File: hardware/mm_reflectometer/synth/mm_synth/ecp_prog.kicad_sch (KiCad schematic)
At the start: 77 parts, among them J1601 USB_C_Receptacle_USB2.0, J1603 JTAG, J1604 Flash, SW1601 SW_Push, SW1602 SW_Push, U1601 ECP5U_25_CABGA256, U1602 93LC56C, U1603 TPD3S014, U1604 FT2232HQ, U1605 W25Q32JVSS, Y1601 7M-12.000MAAJ

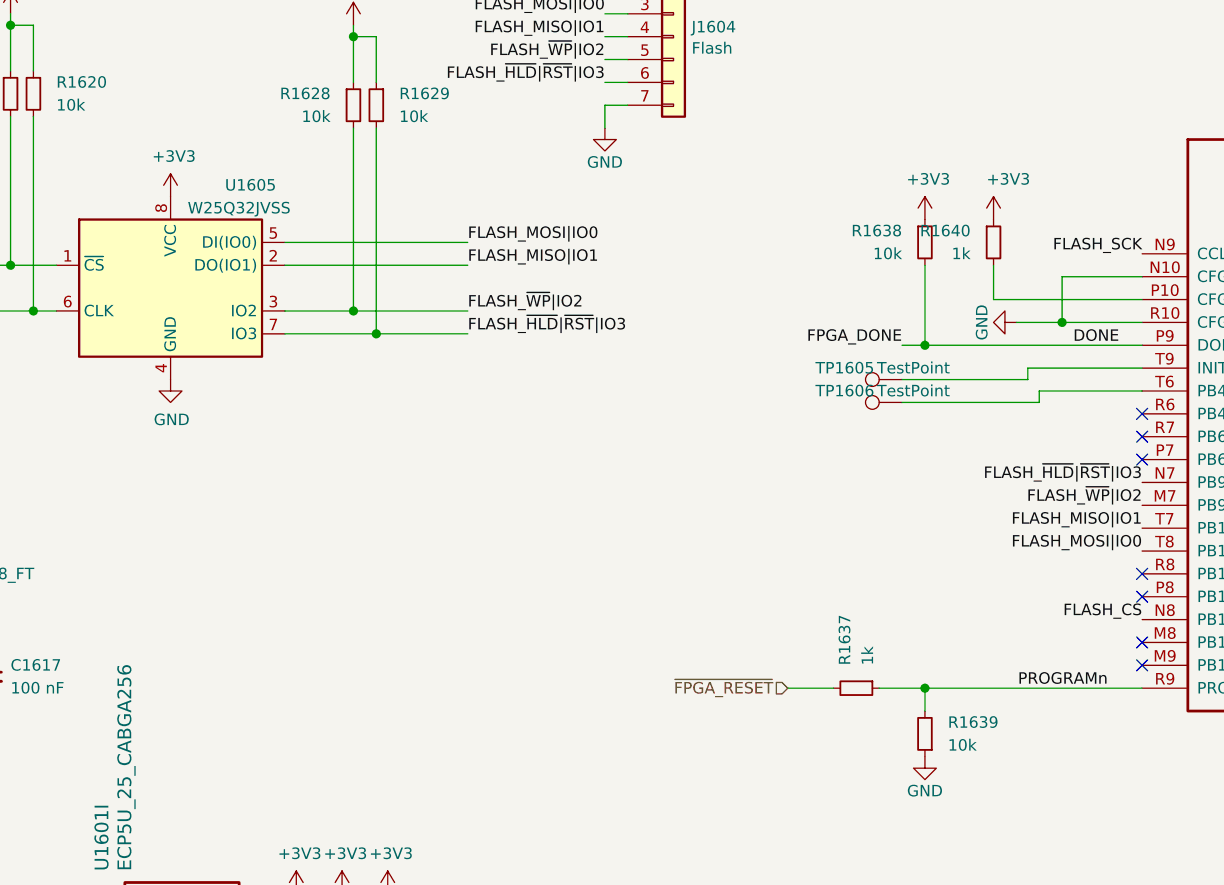
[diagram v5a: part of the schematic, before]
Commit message: created HUSB238 eval board, added clock splitter to mm synth
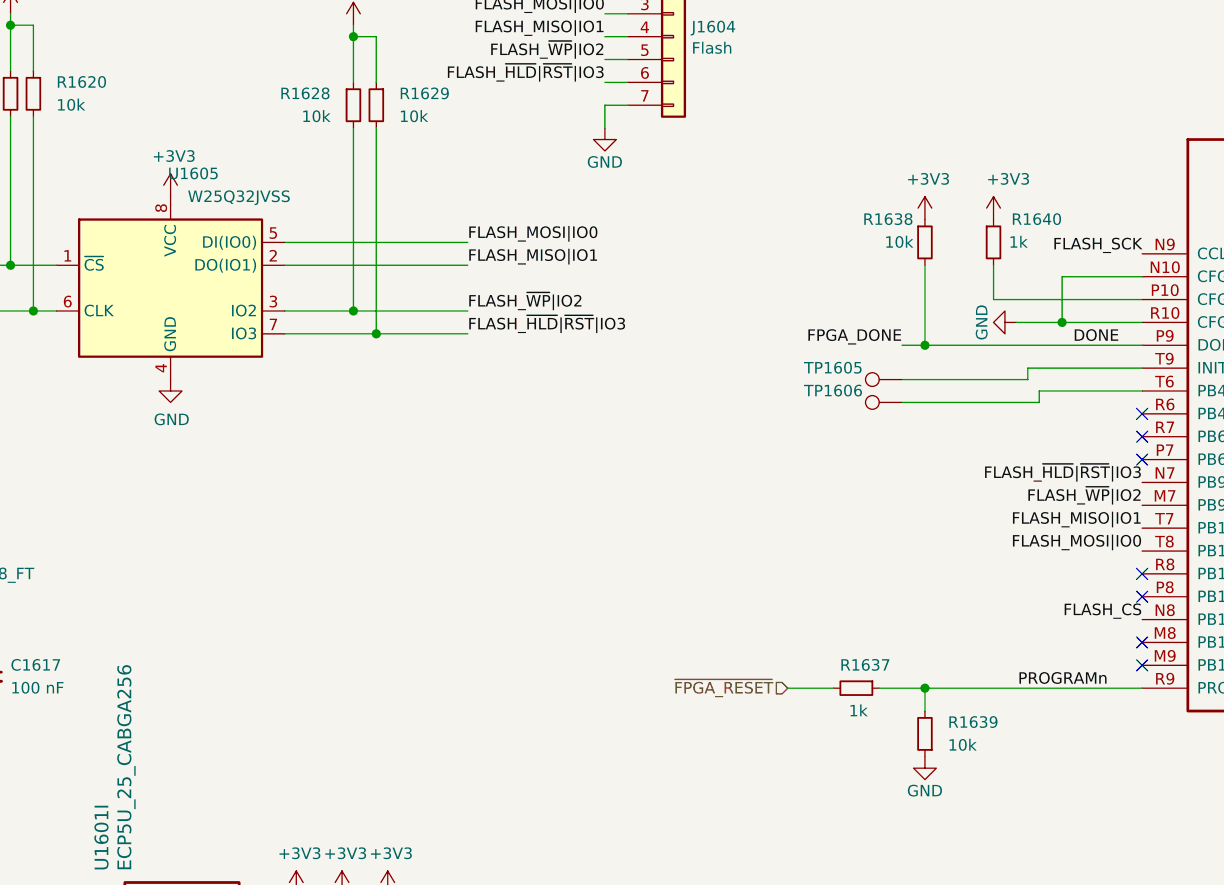
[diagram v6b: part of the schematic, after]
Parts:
- TP1605, TP1606: now left out of the parts list
- U1605: footprint Package_SON:WSON-8-1EP_6x5mm_P1.27mm_EP3.4x4mm -> Package_SO:SOIC-8_5.23x5.23mm_P1.27mm; Notes Flash schematic and symbol adapted from Greg Davill's ECPBr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 -> (none)
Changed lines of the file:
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@@
   )
   (symbol (lib_id "Connector:TestPoint") (at 280.67 67.31 90) (unit 1)
-    (in_bom yes) (on_board yes)
-    (property "Reference" "TP1605" (id 0) (at 274.32 66.04 90))
-    (property "Value" "TestPoint" (id 1) (at 281.94 66.04 90))
+    (in_bom no) (on_board yes)
+    (property "Reference" "TP1605" (id 0) (at 273.05 66.04 90))
+    (property "Value" "TestPoint" (id 1) (at 283.21 66.04 90)
+      (effects (font (size 1.27 1.27)) hide)
+    )
     (property "Footprint" "TestPoint:TestPoint_Pad_D1.5mm" (id 2) (at 280.67 62.23 0)
       (effects (font (size 1.27 1.27)) hide)
@@
   )
   (symbol (lib_id "Connector:TestPoint") (at 280.67 69.85 90) (unit 1)
-    (in_bom yes) (on_board yes)
-    (property "Reference" "TP1606" (id 0) (at 274.32 68.58 90))
-    (property "Value" "TestPoint" (id 1) (at 281.94 68.58 90))
+    (in_bom no) (on_board yes)
+    (property "Reference" "TP1606" (id 0) (at 273.05 68.58 90))
+    (property "Value" "TestPoint" (id 1) (at 281.94 68.58 90)
+      (effects (font (size 1.27 1.27)) hide)
+    )
     (property "Footprint" "TestPoint:TestPoint_Pad_D1.5mm" (id 2) (at 280.67 64.77 0)
       (effects (font (size 1.27 1.27)) hide)
@@
   (symbol (lib_id "Device:R_Small") (at 275.59 101.6 270) (unit 1)
     (in_bom yes) (on_board yes)
-    (property "Reference" "R1637" (id 0) (at 274.32 99.06 0)
-      (effects (font (size 1.27 1.27)) (justify right))
-    )
-    (property "Value" "1k" (id 1) (at 276.86 99.06 0)
+    (property "Reference" "R1637" (id 0) (at 279.4 99.06 90)
+      (effects (font (size 1.27 1.27)) (justify right))
+    )
+    (property "Value" "1k" (id 1) (at 276.86 104.14 90)
       (effects (font (size 1.27 1.27)) (justify right))
     )
@@
   (symbol (lib_id "Device:R_Small") (at 283.21 52.07 0) (unit 1)
     (in_bom yes) (on_board yes)
-    (property "Reference" "R1638" (id 0) (at 280.67 50.8 0)
-      (effects (font (size 1.27 1.27)) (justify right))
-    )
-    (property "Value" "10k" (id 1) (at 280.67 53.34 0)
+    (property "Reference" "R1638" (id 0) (at 281.94 49.53 0)
+      (effects (font (size 1.27 1.27)) (justify right))
+    )
+    (property "Value" "10k" (id 1) (at 281.94 52.07 0)
       (effects (font (size 1.27 1.27)) (justify right))
     )
@@
   (symbol (lib_id "Device:R_Small") (at 290.83 52.07 0) (unit 1)
     (in_bom yes) (on_board yes)
-    (property "Reference" "R1640" (id 0) (at 288.29 50.8 0)
-      (effects (font (size 1.27 1.27)) (justify right))
-    )
-    (property "Value" "1k" (id 1) (at 288.29 53.34 0)
+    (property "Reference" "R1640" (id 0) (at 298.45 49.53 0)
+      (effects (font (size 1.27 1.27)) (justify right))
+    )
+    (property "Value" "1k" (id 1) (at 294.64 52.07 0)
       (effects (font (size 1.27 1.27)) (justify right))
     )
@@
   (symbol (lib_id "Memory_Flash:W25Q32JVSS") (at 199.39 57.15 0) (unit 1)
     (in_bom yes) (on_board yes)
-    (property "Reference" "U1605" (id 0) (at 208.28 45.72 0))
-    (property "Value" "W25Q32JVSS" (id 1) (at 207.01 48.26 0))
-    (property "Footprint" "Package_SON:WSON-8-1EP_6x5mm_P1.27mm_EP3.4x4mm" (id 2) (at 199.39 57.15 0)
+    (property "Reference" "U1605" (id 0) (at 201.93 44.45 0))
+    (property "Value" "W25Q32JVSS" (id 1) (at 207.01 46.99 0))
+    (property "Footprint" "Package_SO:SOIC-8_5.23x5.23mm_P1.27mm" (id 2) (at 199.39 57.15 0)
       (effects (font (size 1.27 1.27)) hide)
     )
@@
       (effects (font (size 1.27 1.27)) hide)
     )
-    (property "Notes" "Flash schematic and symbol adapted from Greg Davill's ECPBreaker, CC-BY-SA V4.0" (id 4) (at 199.39 57.15 0)
-      (effects (font (size 1.27 1.27)) hide)
-    )

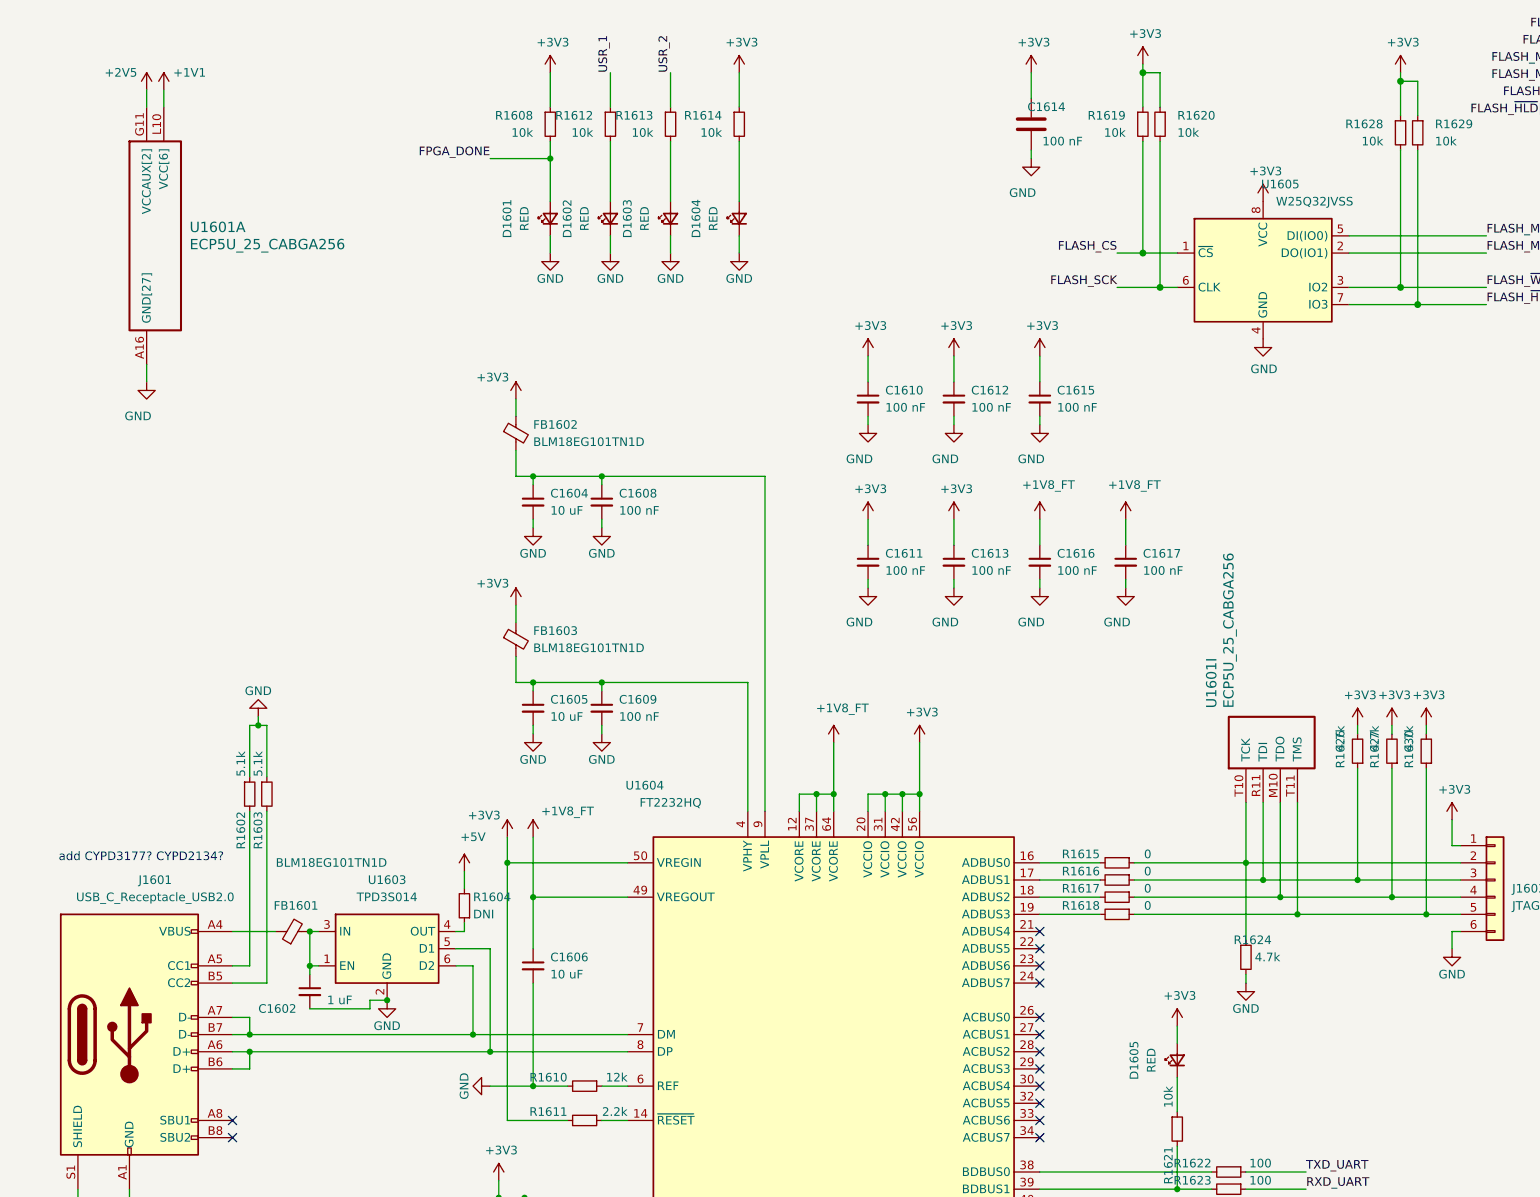
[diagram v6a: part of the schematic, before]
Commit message: more component placement on mm synth
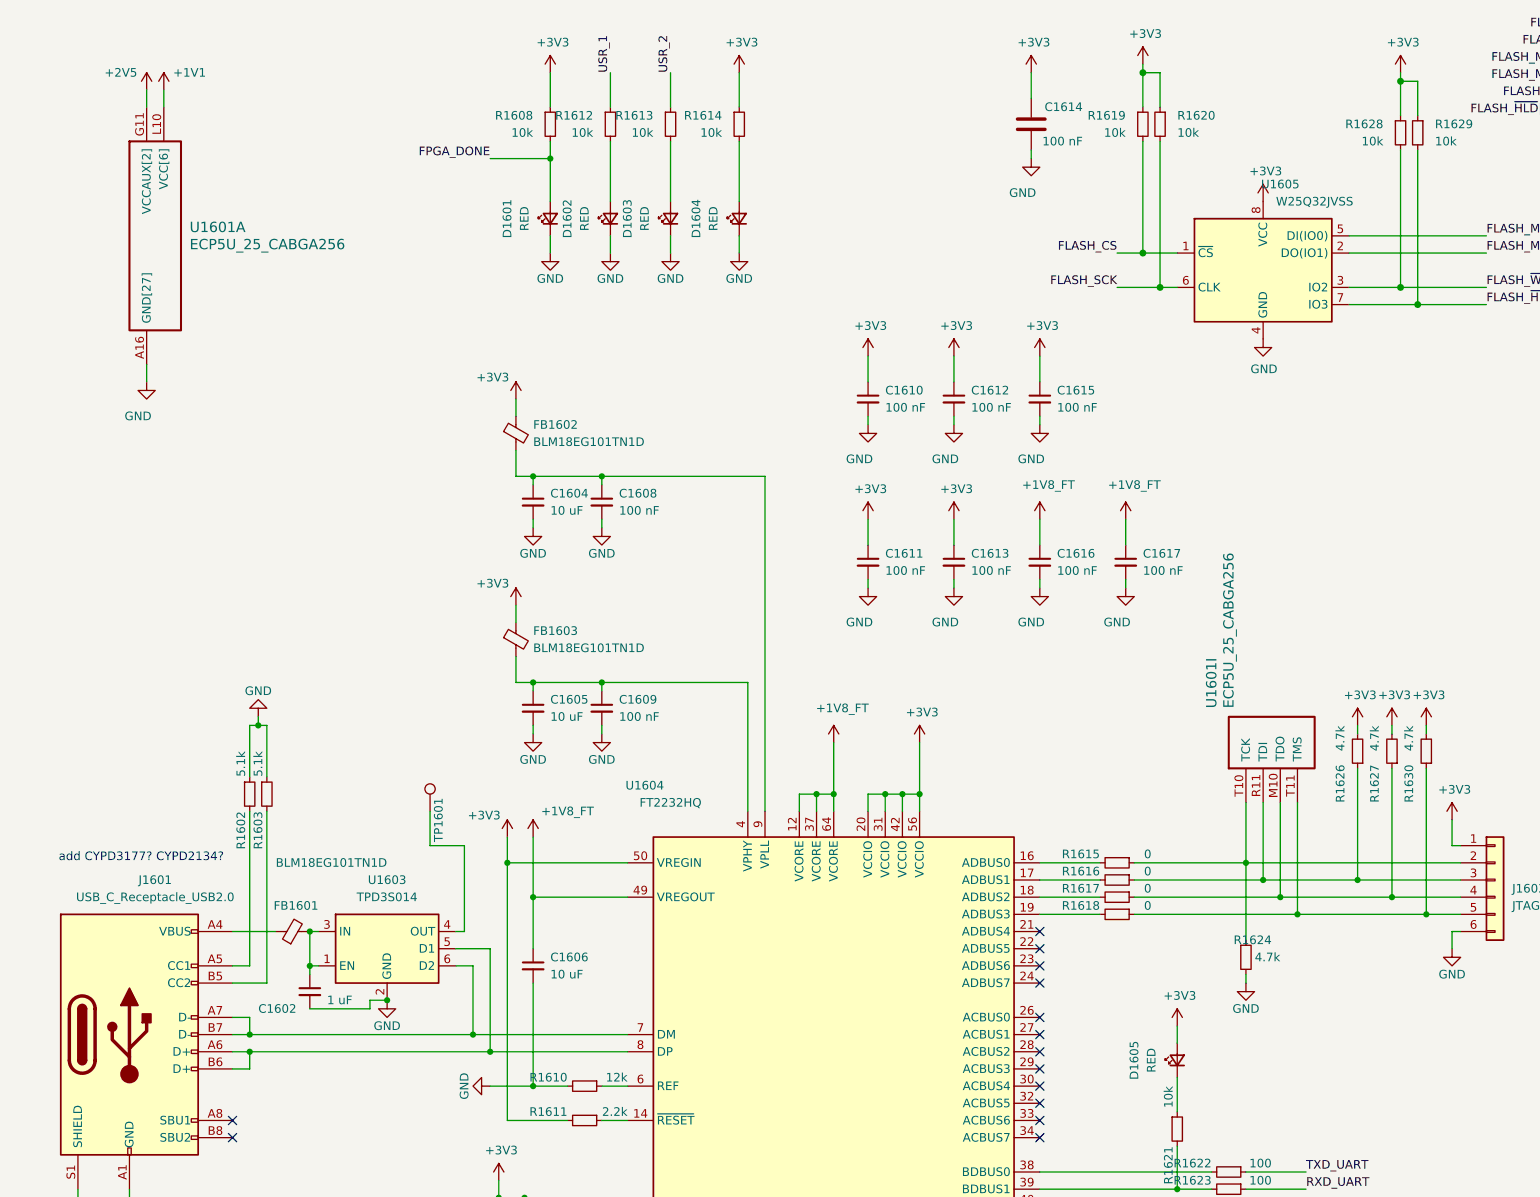
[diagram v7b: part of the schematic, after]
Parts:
- removed R1604: DNI, Resistor_SMD:R_0402_1005Metric, symbol Device:R_Small
- added TP1601: TestPoint, TestPoint:TestPoint_Pad_D1.5mm, symbol Connector:TestPoint
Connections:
- net at U1603.4 (OUT): now also TP1601.1
